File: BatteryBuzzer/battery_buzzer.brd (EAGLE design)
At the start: 33 x 27.9 mm, 26 parts, among them Q1 IRFML8244, Q2 IRFML8244, Q3 P-CHANNEL-MOSFETSOT23-3, Q4 P-CHANNEL-MOSFETSOT23-3, Q5 P-CHANNEL-MOSFETSOT23-3

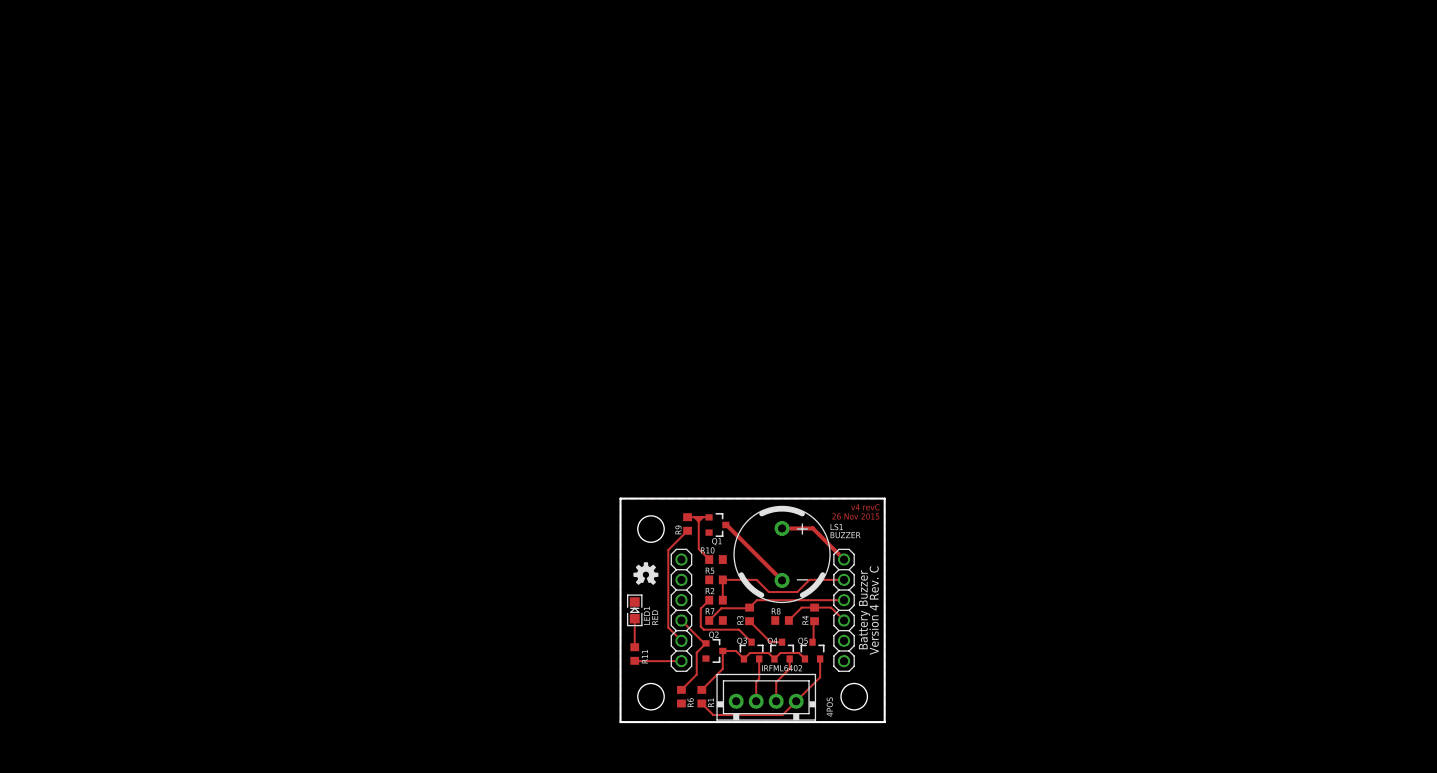
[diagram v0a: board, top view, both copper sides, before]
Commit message: Added 7 segment array & calibration.
also nuked board file, it'd have to change too much anyway.

Have just enough I/O for the calibration button + calibration button
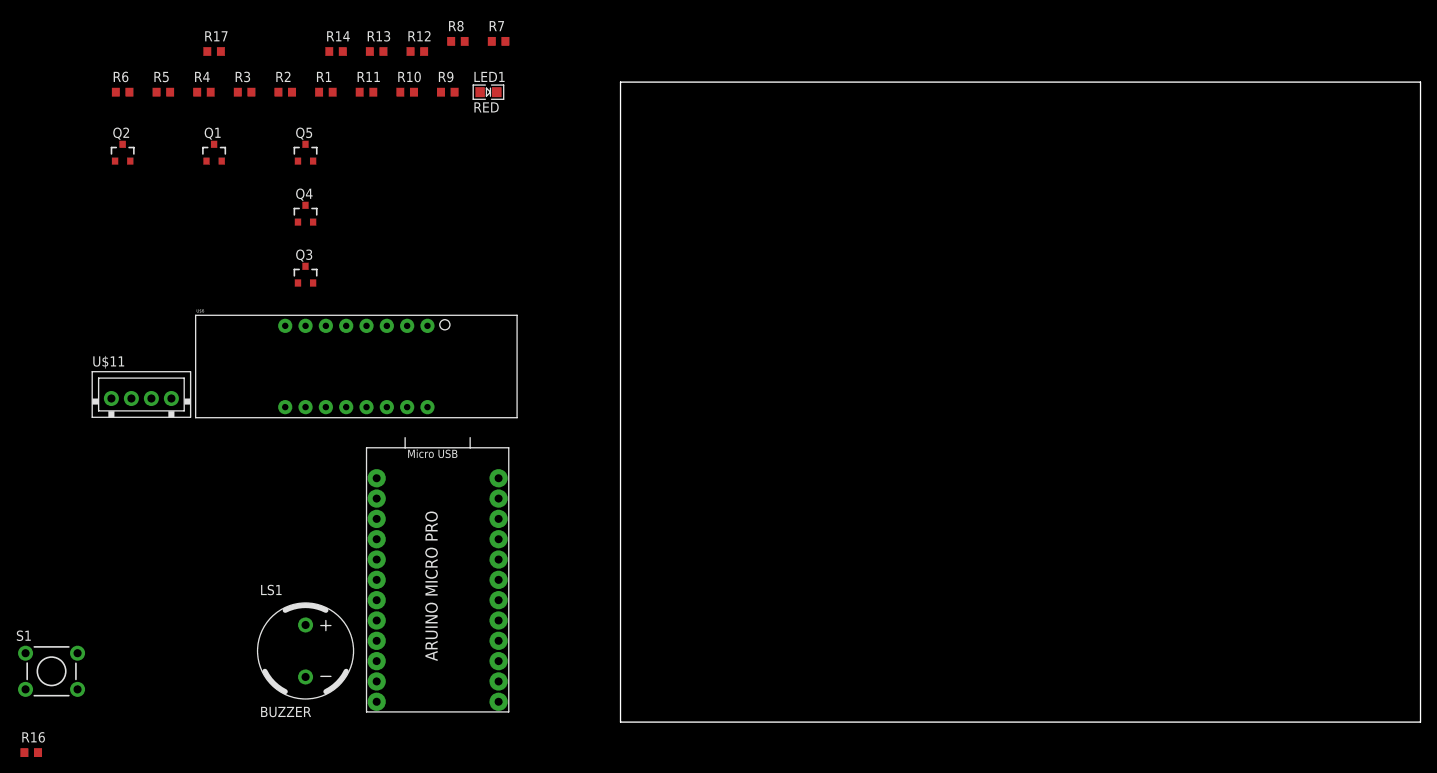
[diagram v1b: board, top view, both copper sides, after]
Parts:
- removed JP1, JP2: (no value), pie:1X06
- removed U$1: (no value), pie:PIE-LOGO-SMALL
- removed U$17, U$2, U$4: (no value), pie:STAND-OFF
- removed U$7: (no value), pie:OSHW-LOGO-S
- added R12, R13, R14, R17: 330, pie:R0603
- added R16: 10k, pie:R0603
- added S1: (no value), pie:TACTILE-PTH
- added U$5: ARDUINO_PRO_MICRO, pie:ARDUINO_PRO_MICRO
- added U$6: 7-SEGMENT-4DIGIT, SparkFun-Displays:7-SEGMENT-4DIGIT-YOUNGSUN
- moved R6 102.9 mm to (-62.2, 78.7), turned to 0 degrees
- moved R4 100.4 mm to (-52.1, 78.7), turned to 0 degrees
- moved Q2 96.6 mm to (-62.2, 71.1), turned to 0 degrees
- moved R5 92.1 mm to (-57.1, 78.7)
- moved R3 90.8 mm to (-47.0, 78.7), turned to 0 degrees
- moved R1 89.0 mm to (-36.8, 78.7), turned to 0 degrees
- moved Q5 88.8 mm to (-39.4, 71.1)
- moved U$11 86.8 mm to (-59.7, 40.6)
- moved R2 83.3 mm to (-41.9, 78.7), turned to 0 degrees
- moved R8 83.0 mm to (-20.3, 85.1)
- moved Q4 80.8 mm to (-39.4, 63.5)
- moved Q1 78.2 mm to (-50.8, 71.1), turned to 0 degrees
- moved R11 77.8 mm to (-31.8, 78.7), turned to 0 degrees
- moved R7 77.3 mm to (-15.2, 85.1), turned to 0 degrees
- moved Q3 72.9 mm to (-39.4, 55.9)
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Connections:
- removed net LED_BUZZER: JP1.6, R11.2
- new net A: U$5.7, U$6.14
- new net B: U$5.8, U$6.16
- new net C: U$5.9, U$6.13
- new net CALIB: R16.1, S1.3, S1.4, U$5.TXO
- new net D: U$5.10, U$6.3
- new net DIG_1: R14.2, U$5.RXI
- new net DIG_2: R12.2, U$5.4
- new net DIG_3: R13.2, U$5.5
- new net DIG_4: R17.2, U$5.6
- new net DP: U$5.A3, U$6.7
- new net E: U$5.16, U$6.5
- new net F: U$5.14, U$6.11
- new net G: U$5.15, U$6.15
- new net N$10: R13.1, U$6.6
- new net N$12: R17.1, U$6.8
- new net N$14: R14.1, U$6.1
- new net N$8: R12.1, U$6.2
- net 5V: now also S1.1, S1.2, U$5.VCC; no longer JP2.1
- net BUZZER_SIGNAL: now also R11.2, U$5.3; no longer JP1.5
- net DIV_EN: now also U$5.2; no longer JP1.4
- net GND: now also R16.2, U$5.GND@0, U$5.GND@1, U$5.GND@2; no longer JP2.6, U$11.1
- net IO0: now also U$5.A0; no longer JP2.2
- net IO1: now also U$5.A1; no longer JP2.3
- net IO2: now also U$5.A2; no longer JP2.4
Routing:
- net BCELL3: track 19.6 -> 0.00 mm
- net IO0: track 19.0 -> 0.00 mm
- net IO1: track 17.9 -> 0.00 mm
- net N$1: track 17.9 -> 0.00 mm
- net BUZZER_SIGNAL: track 15.4 -> 0.00 mm
- net DIV_EN: track 11.3 -> 0.00 mm
- net N$6: track 11.1 -> 0.00 mm
- net N$2: track 10.9 -> 0.00 mm
- net N$5: track 9.90 -> 0.00 mm
- net 5V: track 9.36 -> 0.00 mm
- net IO2: track 8.23 -> 0.00 mm
- net BCELL2: track 5.98 -> 0.00 mm
- net LED_BUZZER: track 5.86 -> 0.00 mm
- net BCELL1: track 5.44 -> 0.00 mm
- net N$3: track 5.15 -> 0.00 mm
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- removed copper zone on layer 1, net GND
- removed copper zone on layer 16, net GND
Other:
- board size 33 x 27.9 mm -> 100 x 80 mm
- board text removed: "(c) Pioneers in Engineering. Design by: Casey D., Jaron A., Abhishyant K., Vincent D., Devin H., and Krystyn N. This design is open source hardware. For more information, visit pioneers.berkeley.edu/opensource."
- board text removed: "4POS"
- board text removed: "Battery Buzzer Version 4 Rev. C"
- board text removed: "IRFML6402"
- board text removed: "v4 revC 26 Nov 2015"
